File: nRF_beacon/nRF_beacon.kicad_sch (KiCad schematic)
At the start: 2 parts, among them J1 USB_C_Receptacle_PowerOnly_6P, J2 Conn_01x03

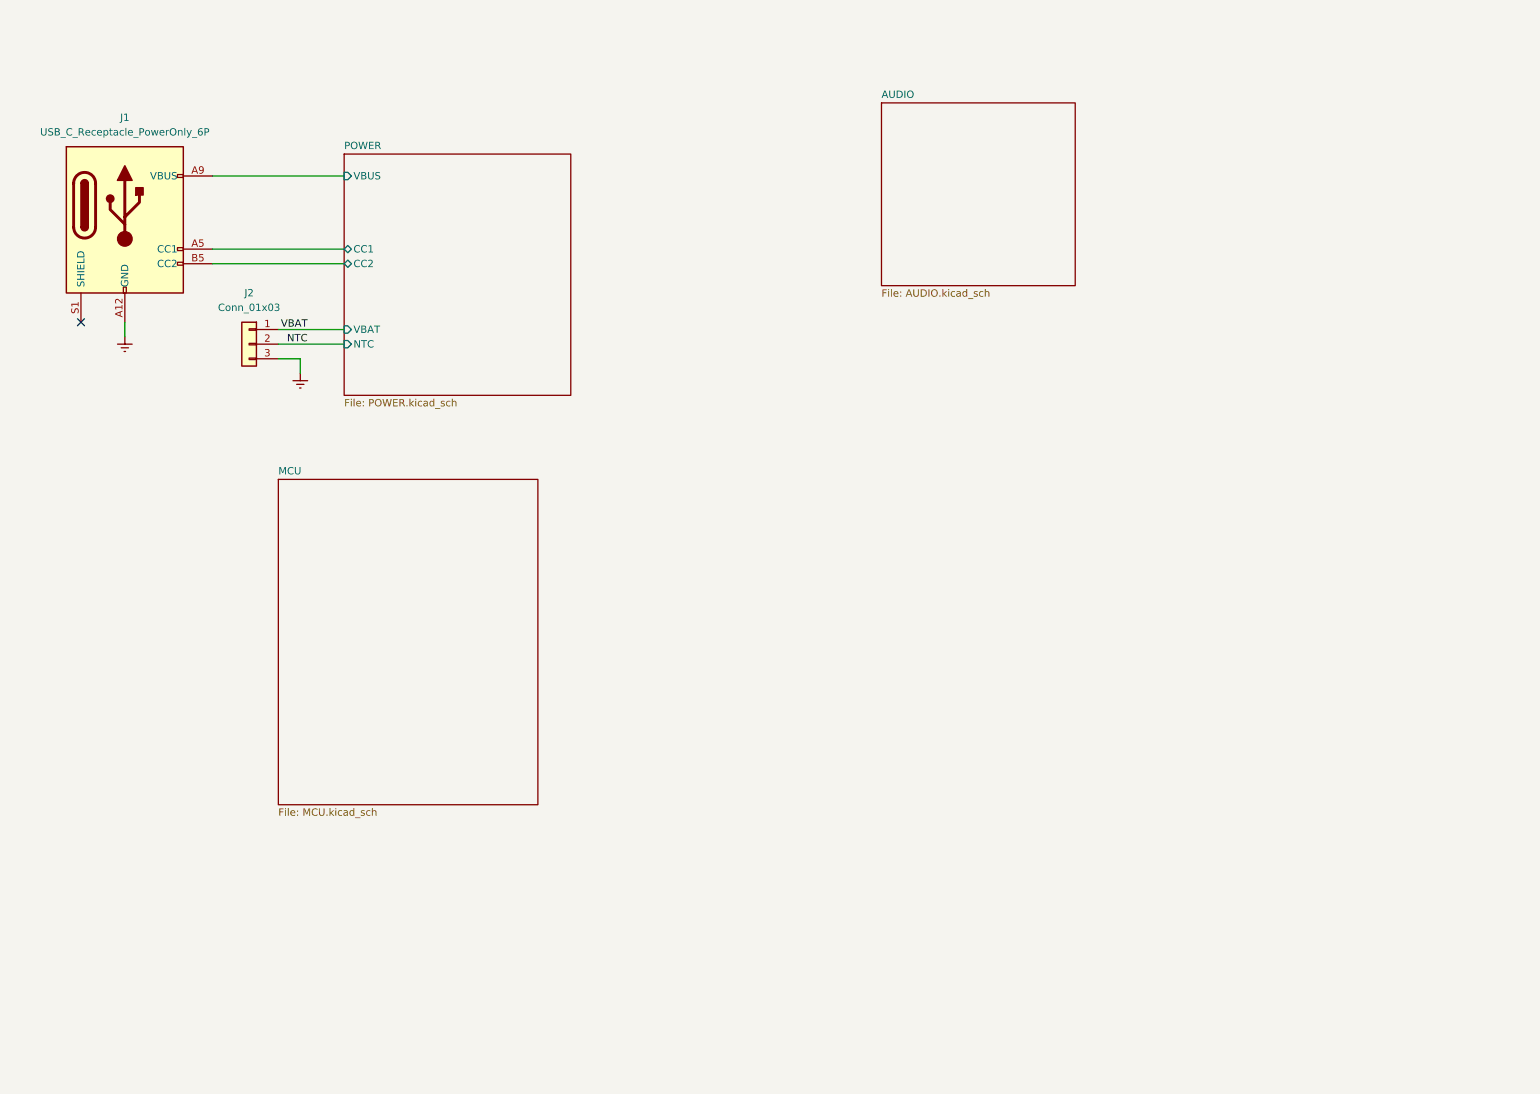
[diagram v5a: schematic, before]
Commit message: Finished typical application nRF. Added audio-block in root sheet.
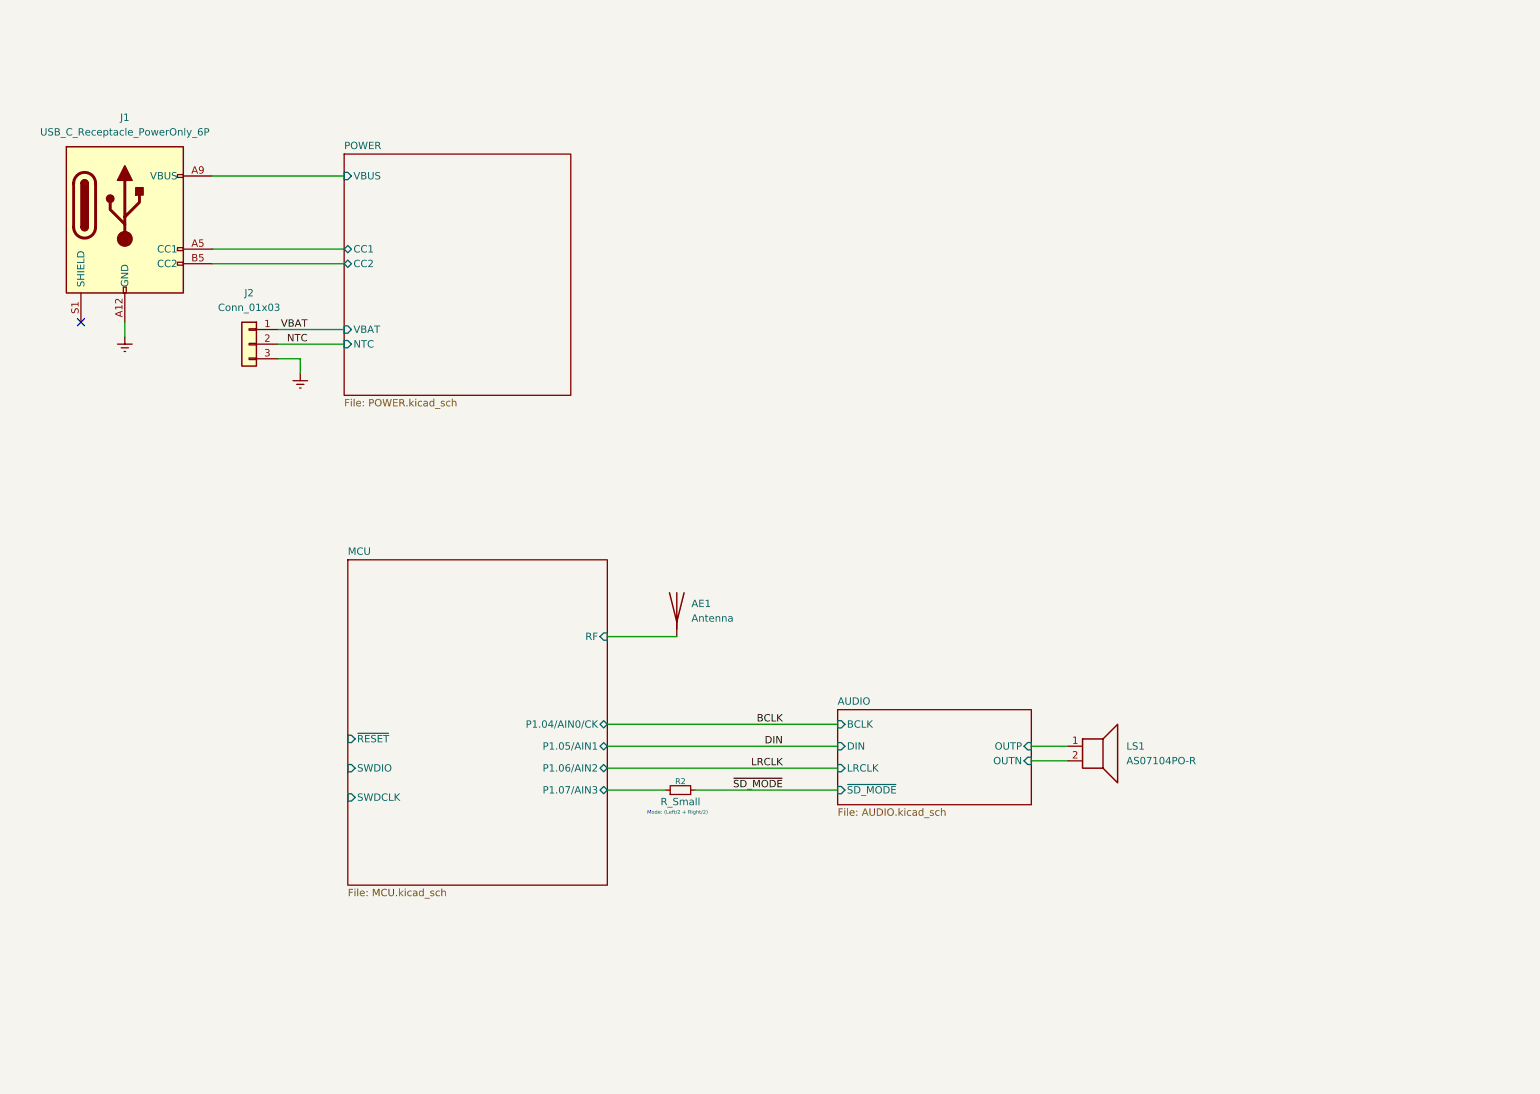
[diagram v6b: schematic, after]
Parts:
- added AE1: Antenna, symbol Device:Antenna
- added LS1: AS07104PO-R, symbol Device:Speaker
- added R2: R_Small, symbol Device:R_Small
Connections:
- new net AUDIO/OUTN: LS1.2
- new net AUDIO/OUTP: LS1.1
- new net MCU/P1.07/AIN3: R2.1
- new net MCU/RF: AE1.1 (A)
- new net ~{SD_MODE}: R2.2
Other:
- sheet AUDIO ports: added BCLK, DIN, LRCLK, OUTN, OUTP, ~{SD_MODE}; removed none
- sheet MCU ports: added P1.04/AIN0/CK, P1.05/AIN1, P1.06/AIN2, P1.07/AIN3, RF, SWDCLK, SWDIO, ~{RESET}; removed none
- note added: "Mode: (Left/2 + Right/2)"

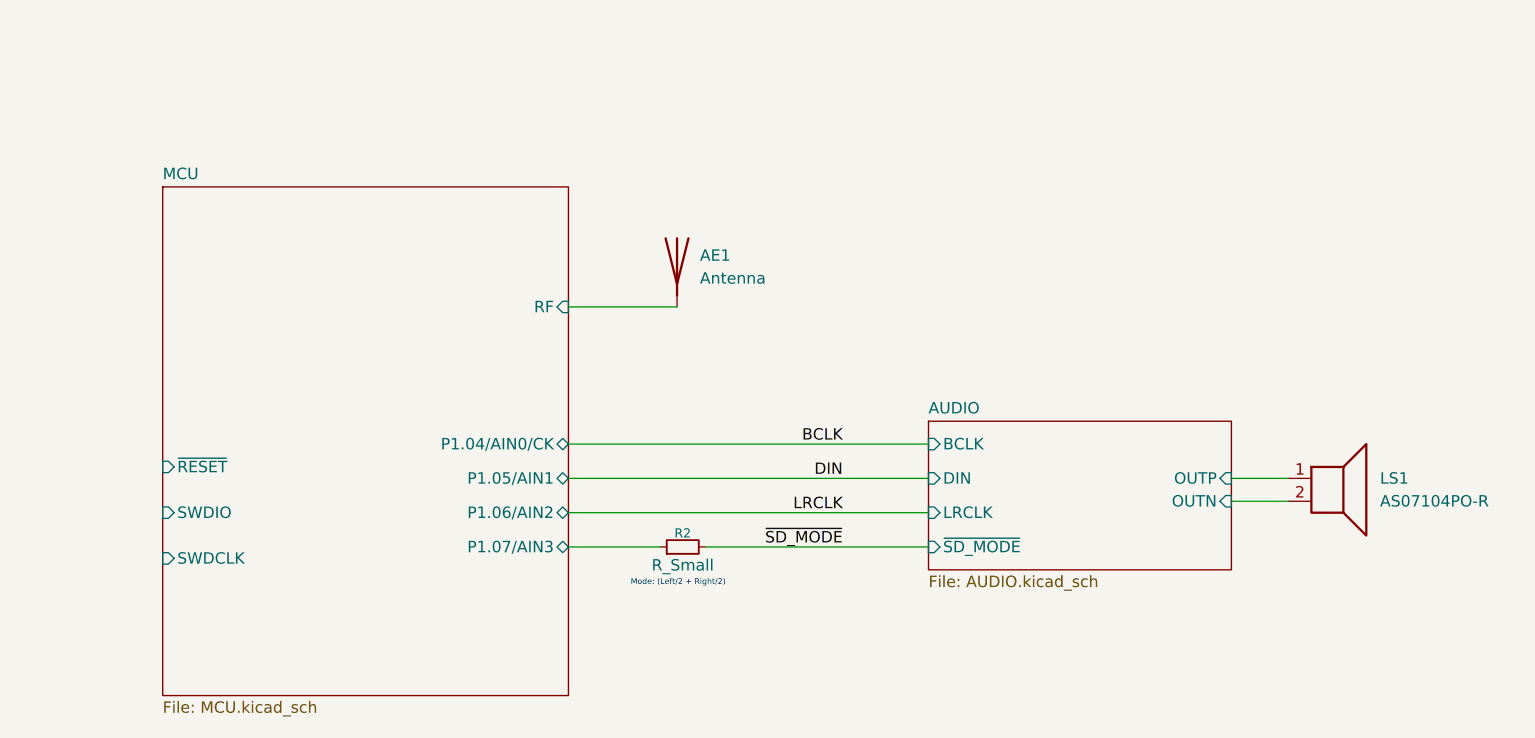
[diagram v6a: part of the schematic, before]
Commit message: small optimizations in root schematics
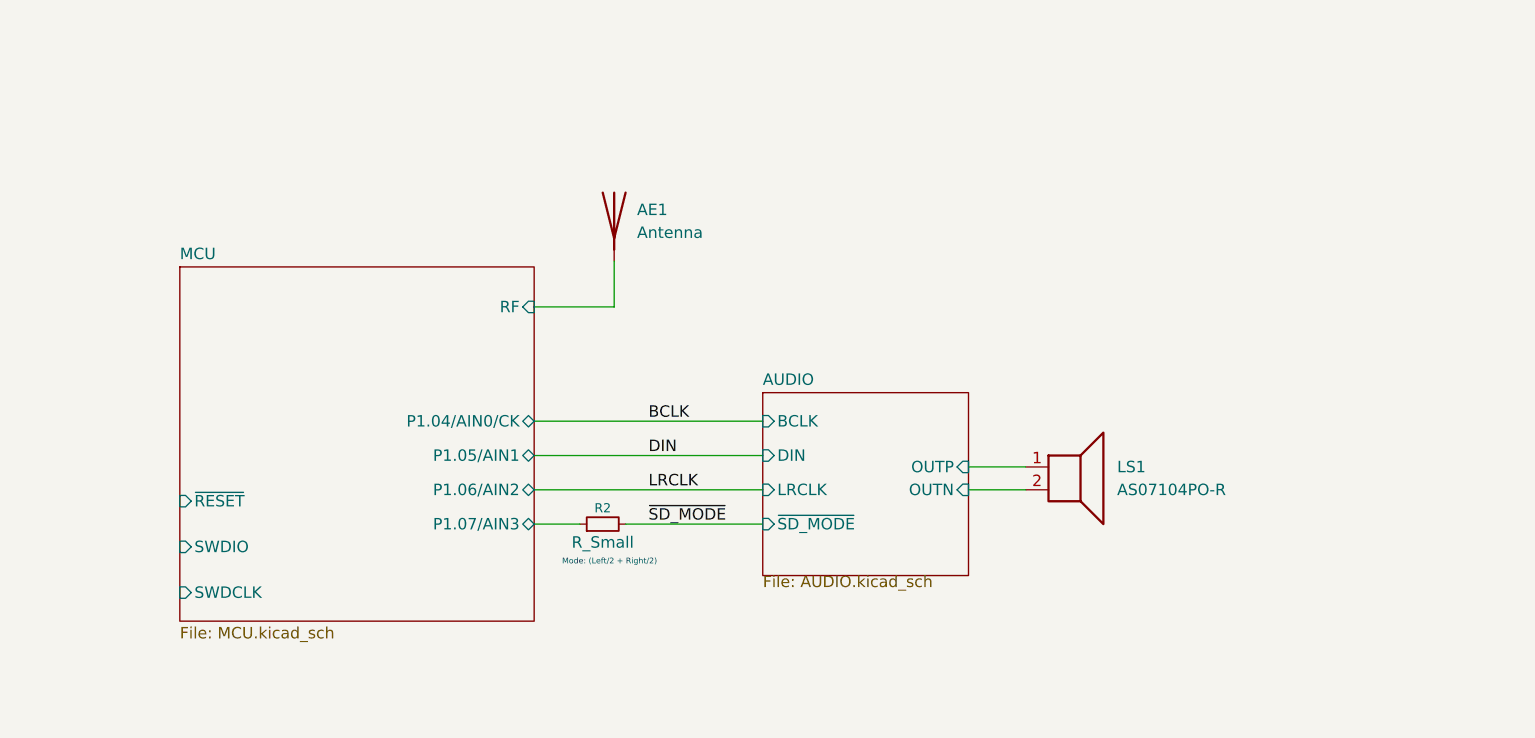
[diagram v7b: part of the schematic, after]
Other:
- sheet MCU ports: added P1.04/AIN0/CK; removed P1.04/AIN0/CK
- moved on the sheet: AE1, LS1

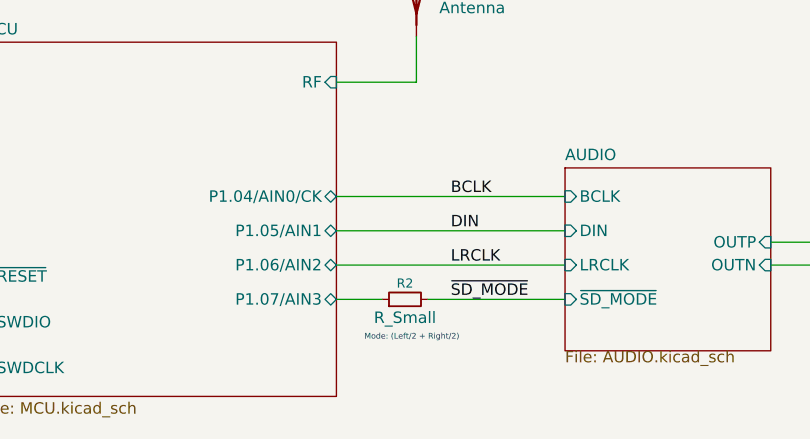
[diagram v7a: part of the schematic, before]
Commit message: Added MPN and footprints for all components on nRF general application
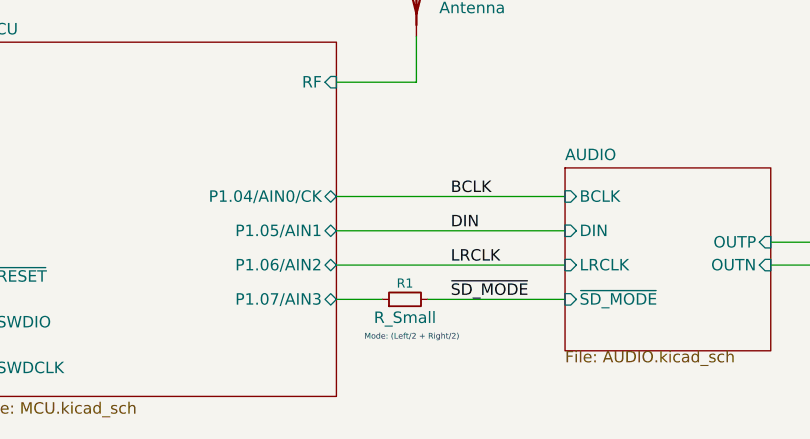
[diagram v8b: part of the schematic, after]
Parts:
- renumbered R2 to R1
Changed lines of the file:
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@@
+			)
+		)
+		(property "MPN" ""
+			(at 31.75 48.26 0)
+			(effects
+				(font
+					(size 1.27 1.27)
+				)
+				(hide yes)
+			)
+		)
+		(property "Price" ""
+			(at 31.75 48.26 0)
+			(effects
+				(font
+					(size 1.27 1.27)
+				)
+				(hide yes)
 			)
 		)
@@
 		(on_board yes)
 		(dnp no)
-		(property "Reference" "R2"
+		(property "Reference" "R1"
 			(at 119.38 143.002 90)
 			(effects
@@
 			)
 		)
+		(property "MPN" ""
+			(at 119.38 144.78 90)
+			(effects
+				(font
+					(size 1.27 1.27)
+				)
+				(hide yes)
+			)
+		)
+		(property "Price" ""
+			(at 119.38 144.78 90)
+			(effects
+				(font
+					(size 1.27 1.27)
+				)
+				(hide yes)
+			)
+		)
 		(pin "2"
 		)
@@
 			(project ""
 				(path "/1290e5f5-b91f-4d6e-b440-6b78e8fdc212"
-					(reference "R2")
+					(reference "R1")
 					(unit 1)
 				)
@@
 		(dnp no)
 		(fields_autoplaced yes)
-		(property "Reference" "#PWR019"
+		(property "Reference" "#PWR01"
 			(at 31.75 74.93 0)
 			(effects
@@
 			(project ""
 				(path "/1290e5f5-b91f-4d6e-b440-6b78e8fdc212"
-					(reference "#PWR019")
+					(reference "#PWR01")
 					(unit 1)
 				)
@@
 			)
 		)
+		(property "MPN" ""
+			(at 53.34 69.85 0)
+			(effects
+				(font
+					(size 1.27 1.27)
+				)
+				(hide yes)
+			)
+		)
+		(property "Price" ""
+			(at 53.34 69.85 0)
+			(effects
+				(font
+					(size 1.27 1.27)
+				)
+				(hide yes)
+			)
+		)
 		(pin "2"
 		)
@@
 			(project ""
 				(path "/1290e5f5-b91f-4d6e-b440-6b78e8fdc212"
+					(reference "J2")
+					(unit 1)
+				)
+				(path "/1290e5f5-b91f-4d6e-b440-6b78e8fdc212/eb04787d-40f4-45c6-8e79-38c58cd136de"
 					(reference "J2")
 					(unit 1)
@@
 		(dnp no)
 		(fields_autoplaced yes)
-		(property "Reference" "#PWR018"
+		(property "Reference" "#PWR02"
 			(at 62.23 81.28 0)
 			(effects
@@
 			(project ""
 				(path "/1290e5f5-b91f-4d6e-b440-6b78e8fdc212"
-					(reference "#PWR018")
+					(reference "#PWR02")
 					(unit 1)
 				)
@@
 			)
 		)
+		(property "MPN" ""
+			(at 120.65 110.49 0)
+			(effects
+				(font
+					(size 1.27 1.27)
+				)
+				(hide yes)
+			)
+		)
+		(property "Price" ""
+			(at 120.65 110.49 0)
+			(effects
+				(font
+					(size 1.27 1.27)
+				)
+				(hide yes)
+			)
+		)
 		(pin "1"
 		)
@@
 			(at 171.45 138.43 0)
 			(effects
+				(font
+					(size 1.27 1.27)
+				)
+				(hide yes)
+			)
+		)
+		(property "MPN" ""
+			(at 171.45 138.43 0)
+			(effects
+				(font
+					(size 1.27 1.27)
+				)
+				(hide yes)
+			)
+		)
+		(property "Price" ""
+			(at 171.45 138.43 0)
+			(effects
